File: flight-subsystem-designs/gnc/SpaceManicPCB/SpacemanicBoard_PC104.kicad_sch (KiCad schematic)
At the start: 3 parts

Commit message: Final Changes
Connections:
- net I2C1_SCL: no longer names the net of H1.43 (Pin_43)
- net I2C1_SDA: no longer names the net of H1.41 (Pin_41)
- no-connect marks 90 -> 92
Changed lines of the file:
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@@
 	(text "The OBC board already\nhas 3k I2C pull up \nresistor, so none needed\nhere"
 		(exclude_from_sim no)
-		(at 75.692 115.062 0)
+		(at 84.328 102.616 0)
 		(effects
 			(font
@@
 	)
 	(no_connect
+		(at 110.49 116.84)
+	)
+	(no_connect
 		(at 123.19 104.14)
 	)
@@
 	)
 	(no_connect
+		(at 110.49 114.3)
+	)
+	(no_connect
 		(at 189.23 106.68)
 	)
@@
 	(wire
 		(pts
-			(xy 99.06 116.84) (xy 110.49 116.84)
-		)
-		(stroke
-			(width 0)
-			(type default)
-		)
-	)
-	(wire
-		(pts
 			(xy 127 127) (xy 130.81 127)
 		)
@@
 		(pts
 			(xy 123.19 127) (xy 127 127)
-		)
-		(stroke
-			(width 0)
-			(type default)
-		)
-	)
-	(wire
-		(pts
-			(xy 99.06 114.3) (xy 110.49 114.3)
 		)
 		(stroke
@@
 		)
 	)
-	(hierarchical_label "I2C1_SCL"
-		(shape input)
-		(at 99.06 116.84 180)
-		(effects
-			(font
-				(size 1.27 1.27)
-			)
-			(justify right)
-		)
-	)
 	(hierarchical_label "CAN_P"
 		(shape input)
@@
 		(effects
 			(font
-				(size 1.27 1.27)
-			)
-			(justify right)
-		)
-	)
-	(hierarchical_label "I2C1_SDA"
-		(shape input)
-		(at 99.06 114.3 180)
-		(effects
-			(font

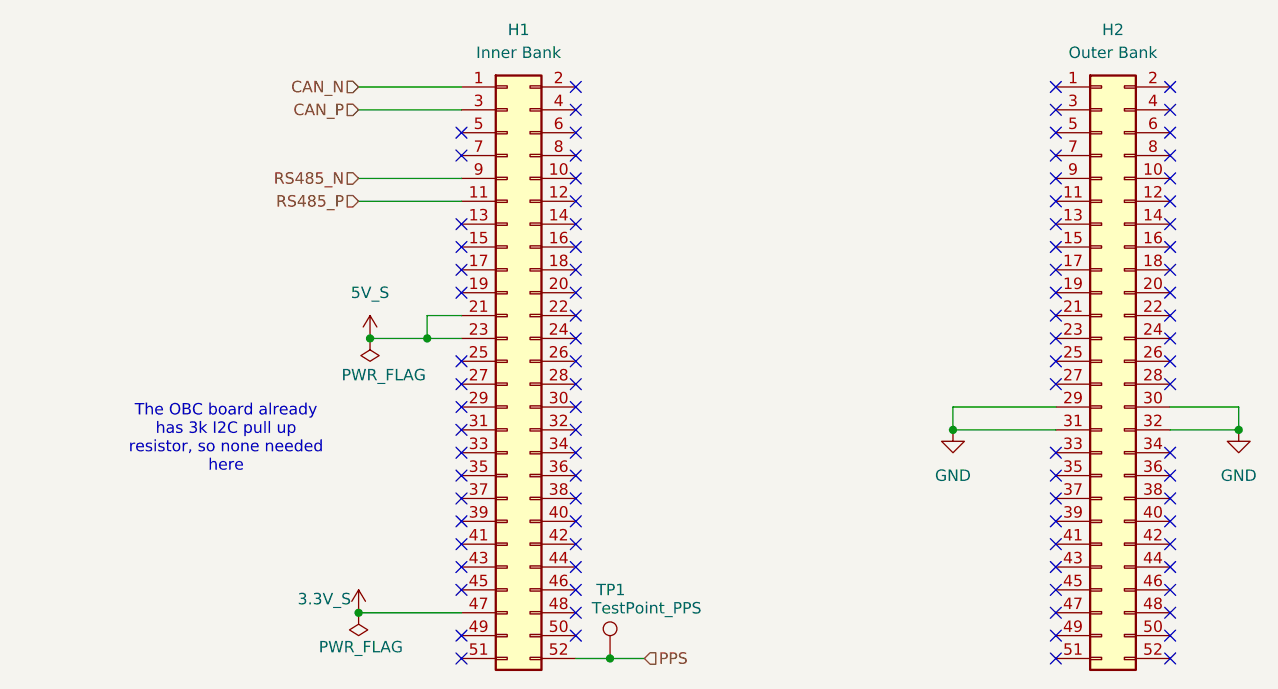
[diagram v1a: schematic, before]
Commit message: Added UART
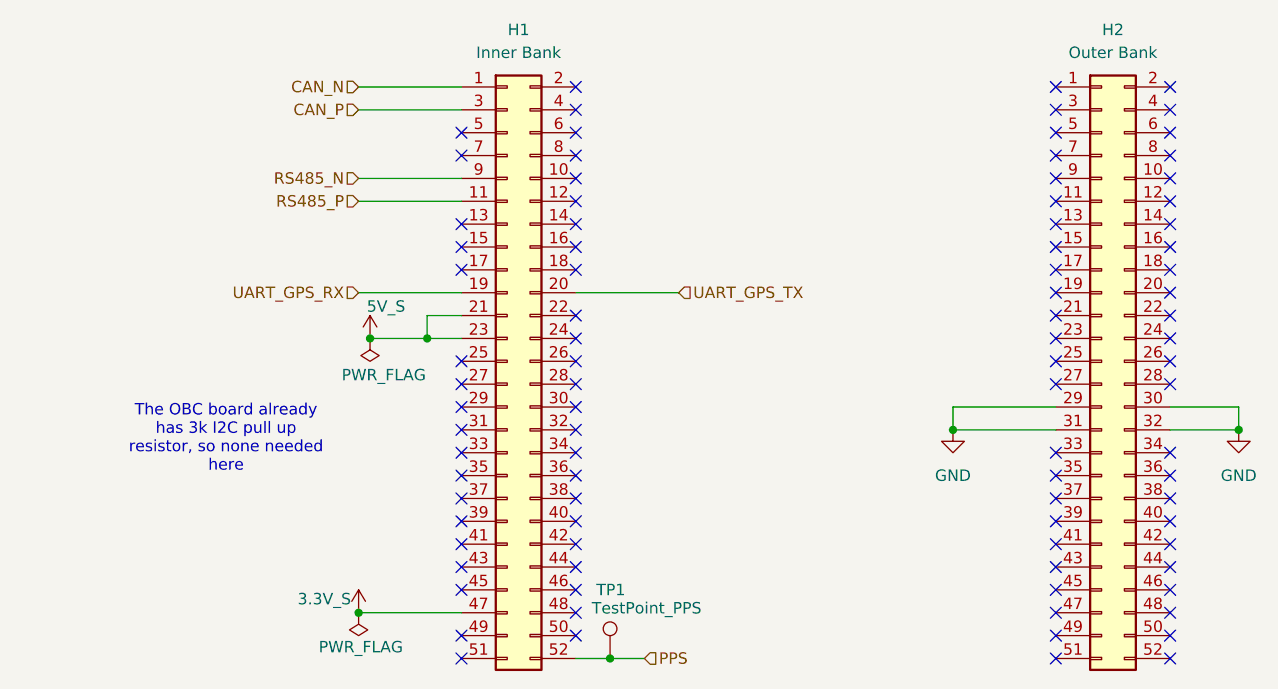
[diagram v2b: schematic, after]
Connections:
- net UART_GPS_RX: now reaches H1.19 (Pin_19)
- net UART_GPS_TX: now reaches H1.20 (Pin_20)
- no-connect marks 92 -> 90
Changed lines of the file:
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@@
-	)
-	(no_connect
-		(at 110.49 86.36)
 	)
 	(no_connect
@@
 	)
 	(no_connect
-		(at 123.19 86.36)
-	)
-	(no_connect
 		(at 110.49 116.84)
 	)
@@
 	(wire
 		(pts
+			(xy 123.19 86.36) (xy 134.62 86.36)
+		)
+		(stroke
+			(width 0)
+			(type default)
+		)
+	)
+	(wire
+		(pts
 			(xy 196.85 99.06) (xy 196.85 101.6)
 		)
@@
 	(wire
 		(pts
+			(xy 99.06 86.36) (xy 110.49 86.36)
+		)
+		(stroke
+			(width 0)
+			(type default)
+		)
+	)
+	(wire
+		(pts
 			(xy 123.19 127) (xy 127 127)
 		)
@@
 		)
 	)
+	(hierarchical_label "UART_GPS_RX"
+		(shape input)
+		(at 99.06 86.36 180)
+		(effects
+			(font
+				(size 1.27 1.27)
+			)
+			(justify right)
+		)
+	)
 	(hierarchical_label "PPS"
 		(shape input)
@@
 			)
 			(justify right)
+		)
+	)
+	(hierarchical_label "UART_GPS_TX"
+		(shape input)
+		(at 134.62 86.36 0)
+		(effects
+			(font
+				(size 1.27 1.27)
+			)
+			(justify left)
 		)
 	)
@@
 		(on_board yes)
 		(dnp no)
-		(fields_autoplaced yes)
 		(property "Reference" "#PWR02"
 			(at 100.33 95.25 0)
@@
 		)
 		(property "Value" "5V_S"
-			(at 100.33 86.36 0)
+			(at 102.108 87.884 0)
 			(effects
 				(font
